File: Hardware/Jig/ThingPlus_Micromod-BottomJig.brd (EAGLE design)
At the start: 124.5 x 83.8 mm, 109 parts, among them J1 USB_A_PTH_MALE, J5 USB_A_SMT_FEMALE, J7 QWIIC_RIGHT_ANGLE, U1 TB_MAIN_BRAIN_CARDEDGE_TB_SIDE, U2 74LVC4066, U4 74LVC4066_MUX_1:1_X4

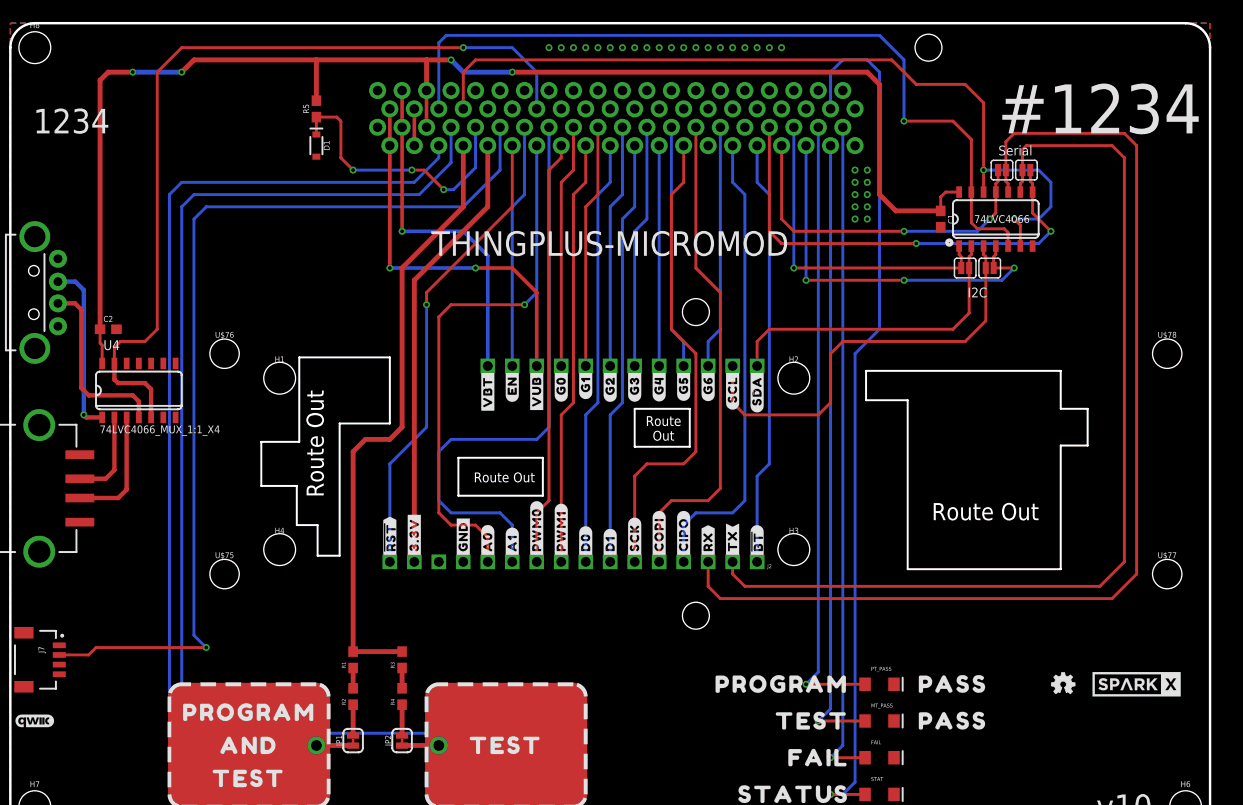
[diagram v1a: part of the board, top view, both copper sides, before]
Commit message: Moved touch pad traces; added missing mounting hole; created top and middle jig boards;
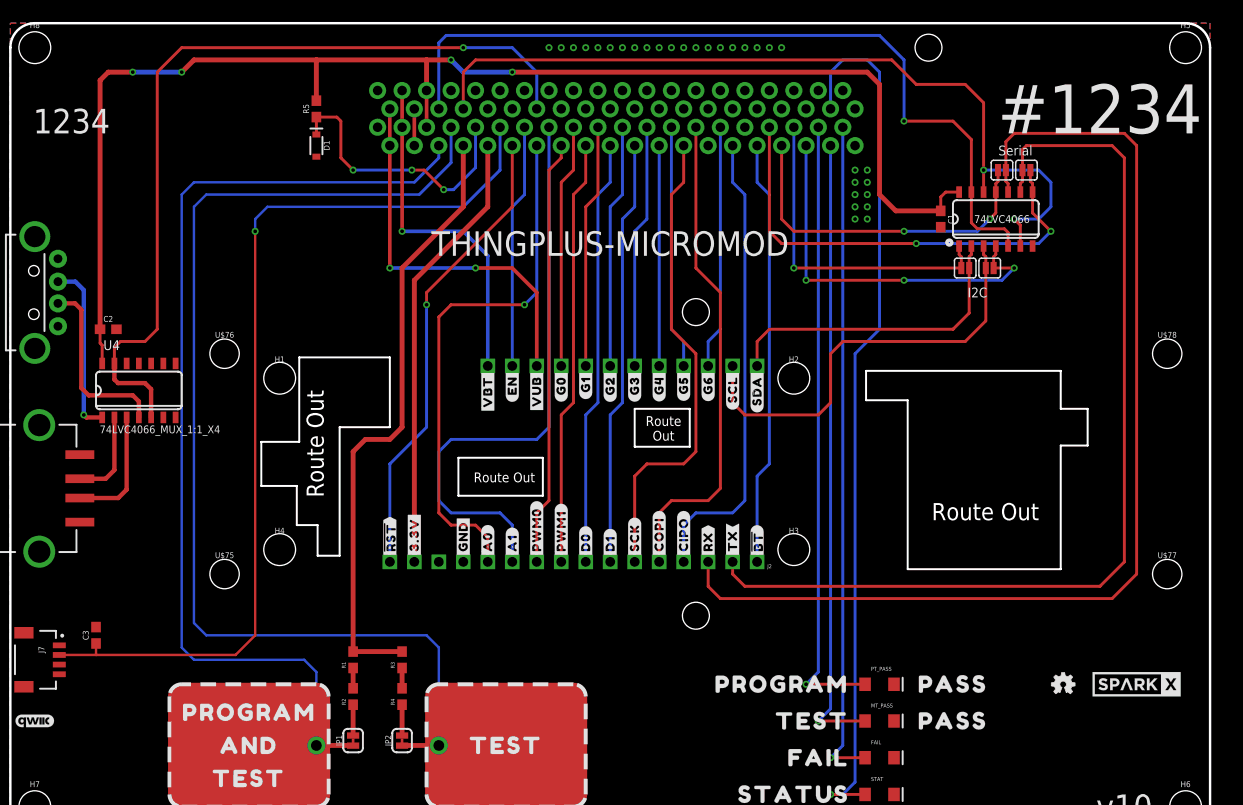
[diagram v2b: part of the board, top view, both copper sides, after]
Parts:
- added C3: 0.1uF, SparkFun-Capacitors:0603
- added H5: STAND-OFF, SparkFun-Hardware:STAND-OFF
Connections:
- net GND: now also C3.2
- net MICROMOD_QWIIC_PWR: now also C3.1
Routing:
- net N$15: track 106.2 -> 103.0 mm
- net N$18: track 118.4 -> 115.9 mm
- net MICROMOD_QWIIC_PWR: track 98.8 -> 97.5 mm
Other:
- outline, holes or cut-outs redrawn
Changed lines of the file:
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@@
 <setting verticaltext="up"/>
 </settings>
-<grid distance="0.05" unitdist="inch" unit="mil" style="lines" multiple="1" display="yes" altdistance="10" altunitdist="mil" altunit="mil"/>
+<grid distance="0.05" unitdist="inch" unit="inch" style="lines" multiple="1" display="yes" altdistance="0.005" altunitdist="inch" altunit="inch"/>
 <layers>
 <layer number="1" name="Top" color="4" fill="1" visible="yes" active="yes"/>
@@
 <layer number="45" name="Holes" color="7" fill="1" visible="yes" active="yes"/>
 <layer number="46" name="Milling" color="3" fill="1" visible="no" active="yes"/>
-<layer number="47" name="Measures" color="7" fill="1" visible="yes" active="yes"/>
+<layer number="47" name="Measures" color="7" fill="1" visible="no" active="yes"/>
 <layer number="48" name="Document" color="7" fill="1" visible="no" active="yes"/>
 <layer number="49" name="Reference" color="7" fill="1" visible="no" active="yes"/>
-<layer number="50" name="Temp" color="13" fill="1" visible="yes" active="yes"/>
+<layer number="50" name="Temp" color="13" fill="1" visible="no" active="yes"/>
 <layer number="51" name="tDocu" color="6" fill="1" visible="yes" active="yes"/>
 <layer number="52" name="bDocu" color="7" fill="1" visible="no" active="yes"/>
@@
 <wire x1="38.862" y1="46.736" x2="38.862" y2="55.499" width="0.2032" layer="20"/>
 <wire x1="38.862" y1="55.499" x2="48.26" y2="55.499" width="0.2032" layer="20"/>
-<wire x1="48.26" y1="55.499" x2="48.26" y2="48.641" width="0.2032" layer="20"/>
-<wire x1="48.26" y1="48.641" x2="43.053" y2="48.641" width="0.2032" layer="20"/>
-<wire x1="43.053" y1="48.641" x2="43.053" y2="34.925" width="0.2032" layer="20"/>
+<wire x1="48.26" y1="55.499" x2="48.26" y2="48.26" width="0.2032" layer="20"/>
+<wire x1="48.26" y1="48.26" x2="43.053" y2="48.26" width="0.2032" layer="20"/>
+<wire x1="43.053" y1="48.26" x2="43.053" y2="34.925" width="0.2032" layer="20"/>
 <wire x1="34.925" y1="46.736" x2="34.925" y2="42.164" width="0.2032" layer="20"/>
 <wire x1="34.925" y1="42.164" x2="38.608" y2="42.164" width="0.2032" layer="20"/>
@@
 <attribute name="VALUE" x="19.05" y="57.658" size="0.6096" layer="27" font="vector" ratio="20" align="top-center"/>
 </element>
+<element name="C3" library="SparkFun-Capacitors" package="0603" value="0.1uF" x="17.78" y="26.67" smashed="yes" rot="R90">
+<attribute name="NAME" x="17.018" y="26.67" size="0.6096" layer="25" font="vector" ratio="20" rot="R90" align="bottom-center"/>
+<attribute name="PROD_ID" value="CAP-00810" x="17.78" y="26.67" size="1.778" layer="27" font="vector" ratio="15" rot="R90" display="off"/>
+<attribute name="VALUE" x="18.542" y="26.67" size="0.6096" layer="27" font="vector" ratio="20" rot="R90" align="top-center"/>
+</element>
+<element name="H5" library="SparkFun-Hardware" package="STAND-OFF" value="STAND-OFF" x="130.81" y="87.63" smashed="yes">
+<attribute name="NAME" x="130.81" y="89.662" size="0.6096" layer="25" font="vector" ratio="20" align="bottom-center"/>
+<attribute name="VALUE" x="130.81" y="85.598" size="0.6096" layer="27" font="vector" ratio="20" align="top-center"/>
+</element>
 </elements>
 <signals>
@@
 <contactref element="J2" pad="13"/>
 <contactref element="U2" pad="7"/>
-<polygon width="0.2032" layer="1" isolate="0.3048">
+<polygon width="0.2032" layer="1" isolate="0.2032">
 <vertex x="8.89" y="90.17"/>
 <vertex x="133.35" y="90.17"/>
@@
 <vertex x="8.89" y="6.35"/>
 </polygon>
-<polygon width="0.2032" layer="16" isolate="0.3048">
+<polygon width="0.2032" layer="16" isolate="0.2032">
 <vertex x="8.89" y="90.17"/>
 <vertex x="133.35" y="90.17"/>
@@
 <via x="78.74" y="87.63" extent="1-16" drill="0.381"/>
 <via x="80.01" y="87.63" extent="1-16" drill="0.381"/>
+<contactref element="C3" pad="2"/>
 </signal>
 <signal name="MICROMOD_PWM0">
@@
 <wire x1="59.69" y1="79.375" x2="59.69" y2="74.93" width="0.3048" layer="16"/>
 <wire x1="59.69" y1="74.93" x2="55.88" y2="71.12" width="0.3048" layer="16"/>
-<wire x1="55.88" y1="71.12" x2="29.21" y2="71.12" width="0.3048" layer="16"/>
-<wire x1="29.21" y1="71.12" x2="27.94" y2="69.85" width="0.3048" layer="16"/>
-<wire x1="27.94" y1="69.85" x2="27.94" y2="26.67" width="0.3048" layer="16"/>
-<wire x1="27.94" y1="26.67" x2="29.21" y2="25.4" width="0.3048" layer="16"/>
-<via x="29.21" y="25.4" extent="1-16" drill="0.381"/>
-<wire x1="29.21" y1="25.4" x2="17.78" y2="25.4" width="0.3048" layer="1"/>
-<wire x1="17.78" y1="25.4" x2="17.01" y2="24.63" width="0.3048" layer="1"/>
-<wire x1="17.01" y1="24.63" x2="13.97" y2="24.63" width="0.3048" layer="1"/>
+<wire x1="55.88" y1="71.12" x2="35.56" y2="71.12" width="0.254" layer="16"/>
+<wire x1="34.29" y1="69.85" x2="35.56" y2="71.12" width="0.254" layer="16"/>
+<contactref element="C3" pad="1"/>
+<wire x1="13.97" y1="24.63" x2="17.78" y2="24.63" width="0.254" layer="1"/>
+<wire x1="17.78" y1="24.63" x2="32.25" y2="24.63" width="0.254" layer="1"/>
+<wire x1="32.25" y1="24.63" x2="34.29" y2="26.67" width="0.254" layer="1"/>
+<wire x1="34.29" y1="26.67" x2="34.29" y2="68.58" width="0.254" layer="1"/>
+<via x="34.29" y="68.58" extent="1-16" drill="0.381"/>
+<wire x1="34.29" y1="68.58" x2="34.29" y2="69.85" width="0.254" layer="16"/>
+<wire x1="17.78" y1="25.82" x2="17.78" y2="24.63" width="0.254" layer="1"/>
 </signal>
 <signal name="PT_PASS_LED">
@@
 <wire x1="40.64" y1="15.24" x2="44.4373" y2="15.24" width="0.508" layer="1"/>
 <wire x1="44.4373" y1="15.24" x2="44.45" y2="15.2273" width="0.508" layer="1"/>
-<wire x1="40.64" y1="15.24" x2="26.67" y2="15.24" width="0.3048" layer="16"/>
-<wire x1="26.67" y1="15.24" x2="25.4" y2="16.51" width="0.3048" layer="16"/>
-<wire x1="25.4" y1="16.51" x2="25.4" y2="72.39" width="0.3048" layer="16"/>
-<wire x1="25.4" y1="72.39" x2="26.67" y2="73.66" width="0.3048" layer="16"/>
-<wire x1="26.67" y1="73.66" x2="50.8" y2="73.66" width="0.3048" layer="16"/>
 <wire x1="53.34" y1="76.2" x2="50.8" y2="73.66" width="0.3048" layer="16"/>
 <wire x1="53.34" y1="76.2" x2="53.34" y2="77.47" width="0.3048" layer="16"/>
+<wire x1="50.8" y1="73.66" x2="27.94" y2="73.66" width="0.254" layer="16"/>
+<wire x1="27.94" y1="73.66" x2="26.67" y2="72.39" width="0.254" layer="16"/>
+<wire x1="26.67" y1="72.39" x2="26.67" y2="25.4" width="0.254" layer="16"/>
+<wire x1="26.67" y1="25.4" x2="27.94" y2="24.13" width="0.254" layer="16"/>
+<wire x1="27.94" y1="24.13" x2="39.37" y2="24.13" width="0.254" layer="16"/>
+<wire x1="39.37" y1="24.13" x2="40.64" y2="22.86" width="0.254" layer="16"/>
+<wire x1="40.64" y1="22.86" x2="40.64" y2="15.24" width="0.254" layer="16"/>
 </signal>
 <signal name="N$16" class="3">
@@
 <wire x1="49.53" y1="15.2273" x2="49.5427" y2="15.24" width="0.508" layer="1"/>
 <wire x1="49.5427" y1="15.24" x2="53.34" y2="15.24" width="0.508" layer="1"/>
-<wire x1="53.34" y1="15.24" x2="52.07" y2="16.51" width="0.3048" layer="16"/>
-<wire x1="52.07" y1="16.51" x2="27.94" y2="16.51" width="0.3048" layer="16"/>
-<wire x1="27.94" y1="16.51" x2="26.67" y2="17.78" width="0.3048" layer="16"/>
-<wire x1="26.67" y1="17.78" x2="26.67" y2="71.12" width="0.3048" layer="16"/>
-<wire x1="26.67" y1="71.12" x2="27.94" y2="72.39" width="0.3048" layer="16"/>
-<wire x1="27.94" y1="72.39" x2="51.308" y2="72.39" width="0.3048" layer="16"/>
 <wire x1="54.61" y1="75.692" x2="51.308" y2="72.39" width="0.3048" layer="16"/>
 <wire x1="54.61" y1="75.692" x2="54.61" y2="79.375" width="0.3048" layer="16"/>
+<wire x1="51.308" y1="72.39" x2="29.21" y2="72.39" width="0.254" layer="16"/>
+<wire x1="29.21" y1="72.39" x2="27.94" y2="71.12" width="0.254" layer="16"/>
+<wire x1="27.94" y1="71.12" x2="27.94" y2="27.94" width="0.254" layer="16"/>
+<wire x1="27.94" y1="27.94" x2="29.21" y2="26.67" width="0.254" layer="16"/>
+<wire x1="29.21" y1="26.67" x2="52.07" y2="26.67" width="0.254" layer="16"/>
+<wire x1="52.07" y1="26.67" x2="53.34" y2="25.4" width="0.254" layer="16"/>
+<wire x1="53.34" y1="25.4" x2="53.34" y2="15.24" width="0.254" layer="16"/>
 </signal>
 <signal name="J_MICROSD_!CS!">

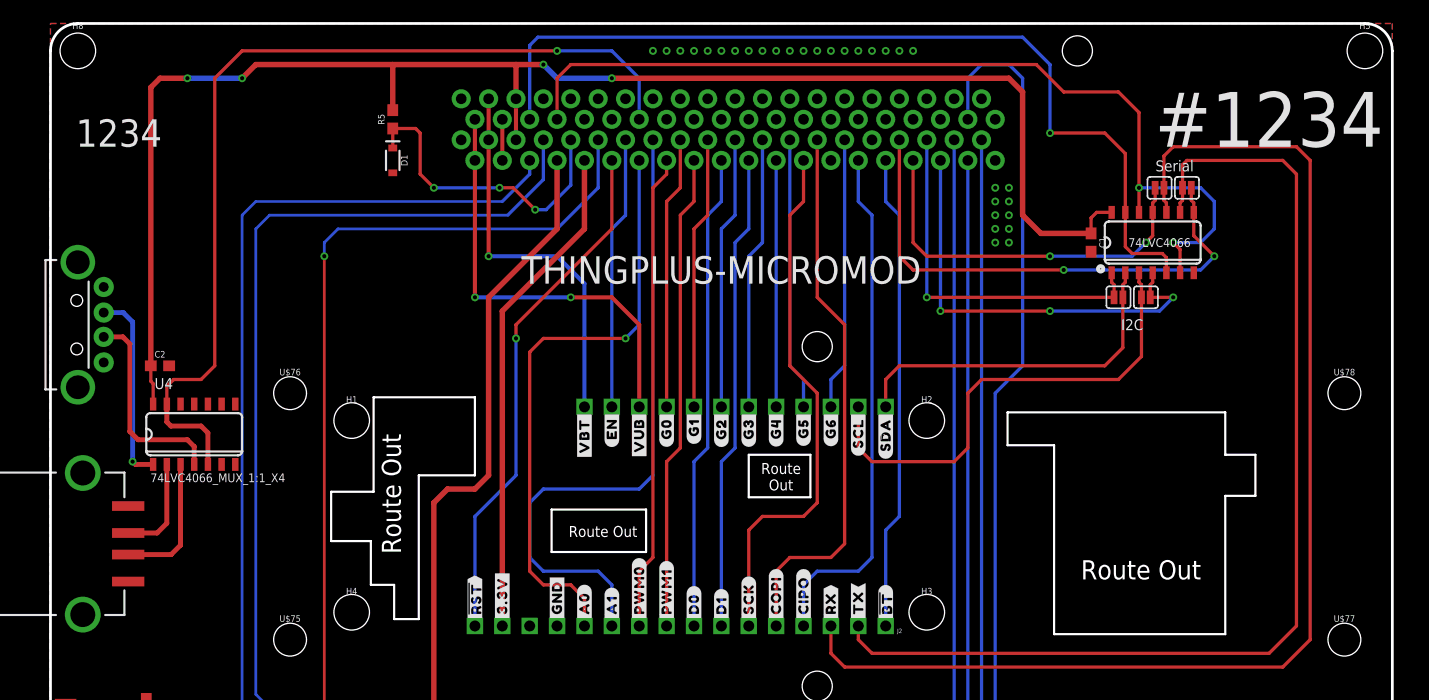
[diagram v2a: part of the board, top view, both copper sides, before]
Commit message: Added milling polygons to bottom and middle jig boards; created Gerber files.
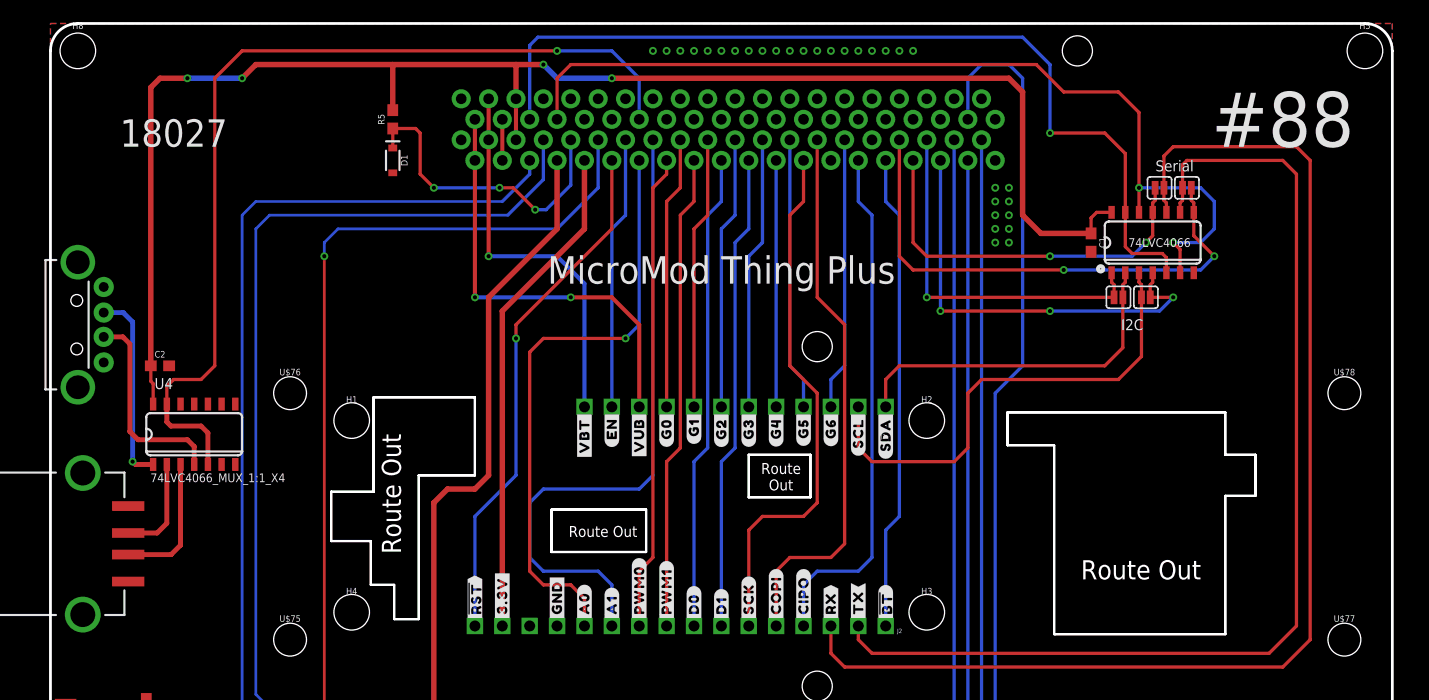
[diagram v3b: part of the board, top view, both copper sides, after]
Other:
- outline, holes or cut-outs redrawn
- board text added: "#88"
- board text added: "18027"
- board text added: "MicroMod Thing Plus"
- board text removed: "#1234"
- board text removed: "1234"
- board text removed: "THINGPLUS-MICROMOD"
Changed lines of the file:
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@@
 <setting verticaltext="up"/>
 </settings>
-<grid distance="0.05" unitdist="inch" unit="inch" style="lines" multiple="1" display="yes" altdistance="0.005" altunitdist="inch" altunit="inch"/>
+<grid distance="50" unitdist="mil" unit="mil" style="lines" multiple="1" display="yes" altdistance="1" altunitdist="mil" altunit="mil"/>
 <layers>
 <layer number="1" name="Top" color="4" fill="1" visible="yes" active="yes"/>
@@
 <layer number="44" name="Drills" color="7" fill="1" visible="no" active="yes"/>
 <layer number="45" name="Holes" color="7" fill="1" visible="yes" active="yes"/>
-<layer number="46" name="Milling" color="3" fill="1" visible="no" active="yes"/>
+<layer number="46" name="Milling" color="3" fill="1" visible="yes" active="yes"/>
 <layer number="47" name="Measures" color="7" fill="1" visible="no" active="yes"/>
 <layer number="48" name="Document" color="7" fill="1" visible="no" active="yes"/>
@@
 <text x="113.157" y="76.962" size="1.016" layer="21" font="vector" ratio="15" rot="R180" align="center">Serial</text>
 <text x="109.22" y="62.23" size="1.016" layer="21" font="vector" ratio="15" rot="R180" align="center">I2C</text>
-<text x="121.92" y="81.28" size="5.08" layer="21" ratio="15" align="center">#1234</text>
-<text x="71.12" y="67.31" size="2.54" layer="21" ratio="15" align="center">THINGPLUS-MICROMOD</text>
-<text x="15.24" y="80.01" size="2.54" layer="21" ratio="15" align="center">1234</text>
+<text x="123.19" y="81.28" size="5.08" layer="21" ratio="15" align="center">#88</text>
+<text x="71.12" y="67.31" size="2.54" layer="21" ratio="15" align="center">MicroMod Thing Plus</text>
+<text x="20.32" y="80.01" size="2.54" layer="21" ratio="15" align="center">18027</text>
 <wire x1="40.767" y1="34.925" x2="43.053" y2="34.925" width="0.2032" layer="20"/>
 <wire x1="40.767" y1="38.1" x2="40.767" y2="34.925" width="0.2032" layer="20"/>
@@
 <text x="76.6500125" y="48.133" size="1.016" layer="20" ratio="15" rot="R180" align="center">Route
 Out</text>
+<polygon width="0.2032" layer="46">
+<vertex x="34.925" y="46.736"/>
+<vertex x="38.862" y="46.736"/>
+<vertex x="38.862" y="55.499"/>
+<vertex x="48.26" y="55.499"/>
+<vertex x="48.26" y="48.26"/>
+<vertex x="43.053" y="48.26"/>
+<vertex x="43.053" y="34.925"/>
+<vertex x="40.767" y="34.925"/>
+<vertex x="40.767" y="38.1"/>
+<vertex x="38.608" y="38.1"/>
+<vertex x="38.608" y="42.164"/>
+<vertex x="34.925" y="42.164"/>
+</polygon>
+<polygon width="0.2032" layer="46">
+<vertex x="55.372" y="45.085"/>
+<vertex x="64.135" y="45.085"/>
+<vertex x="64.135" y="41.148"/>
+<vertex x="55.372" y="41.148"/>
+<vertex x="55.372" y="44.958"/>
+</polygon>
+<polygon width="0.2032" layer="46">
+<vertex x="73.66" y="50.165"/>
+<vertex x="79.375" y="50.165"/>
+<vertex x="79.375" y="46.228"/>
+<vertex x="73.66" y="46.228"/>
+</polygon>
+<polygon width="0.2032" layer="46">
+<vertex x="97.663" y="54.102"/>
+<vertex x="97.663" y="51.054"/>
+<vertex x="101.981" y="51.054"/>
+<vertex x="101.981" y="33.528"/>
+<vertex x="102.108" y="33.528"/>
+<vertex x="117.856" y="33.528"/>
+<vertex x="117.856" y="46.355"/>
+<vertex x="120.65" y="46.355"/>
+<vertex x="120.65" y="50.165"/>
+<vertex x="117.856" y="50.165"/>
+<vertex x="117.856" y="54.102"/>
+</polygon>
 </plain>
 <attributes>
